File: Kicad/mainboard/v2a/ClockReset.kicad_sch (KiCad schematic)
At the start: 23 parts, among them J9 Conn_01x03_Pin, SW1 RESET Switch, U2 74HC14, U3 74HC590, U4 74HC4040, U5 SST39SF, U6 74HC574, Y1 12 Mhz

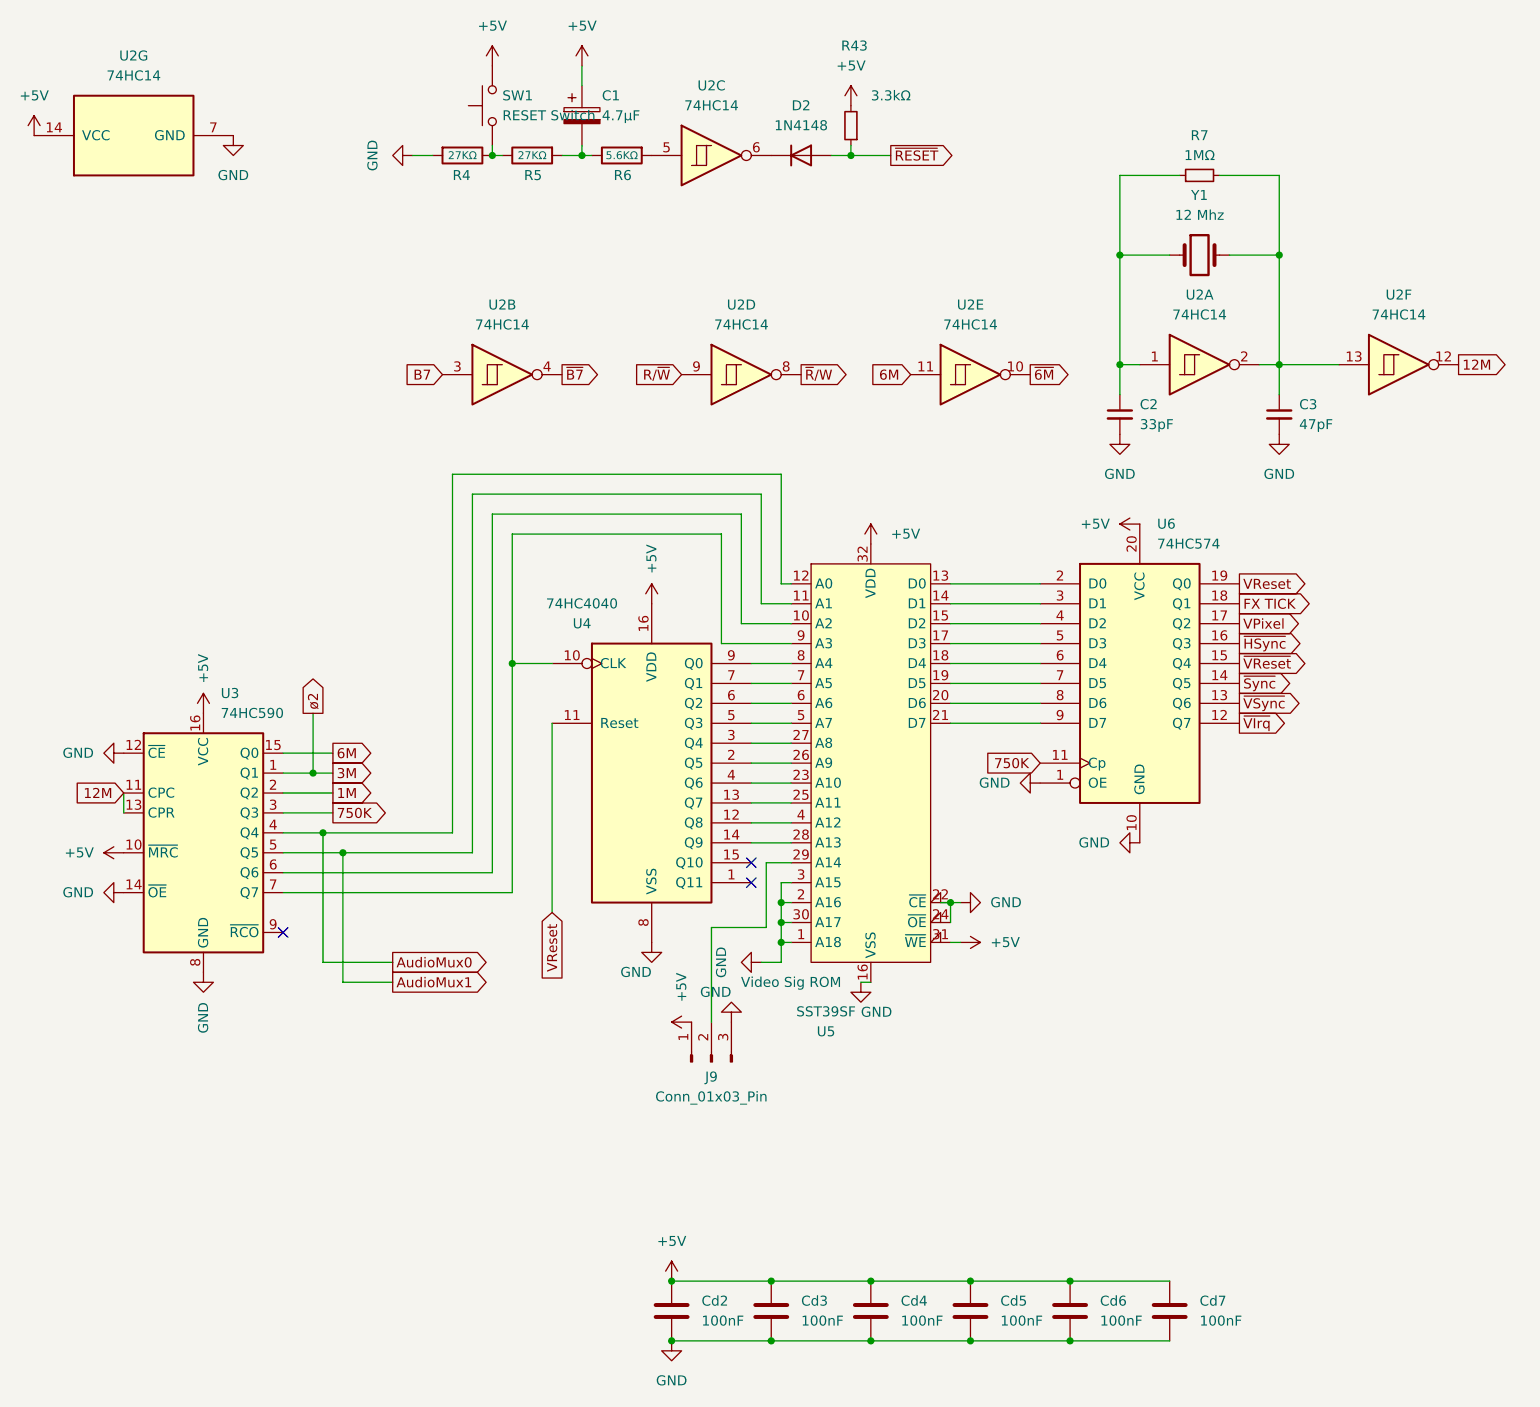
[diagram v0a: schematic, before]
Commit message: Updated pcb files and python scripts
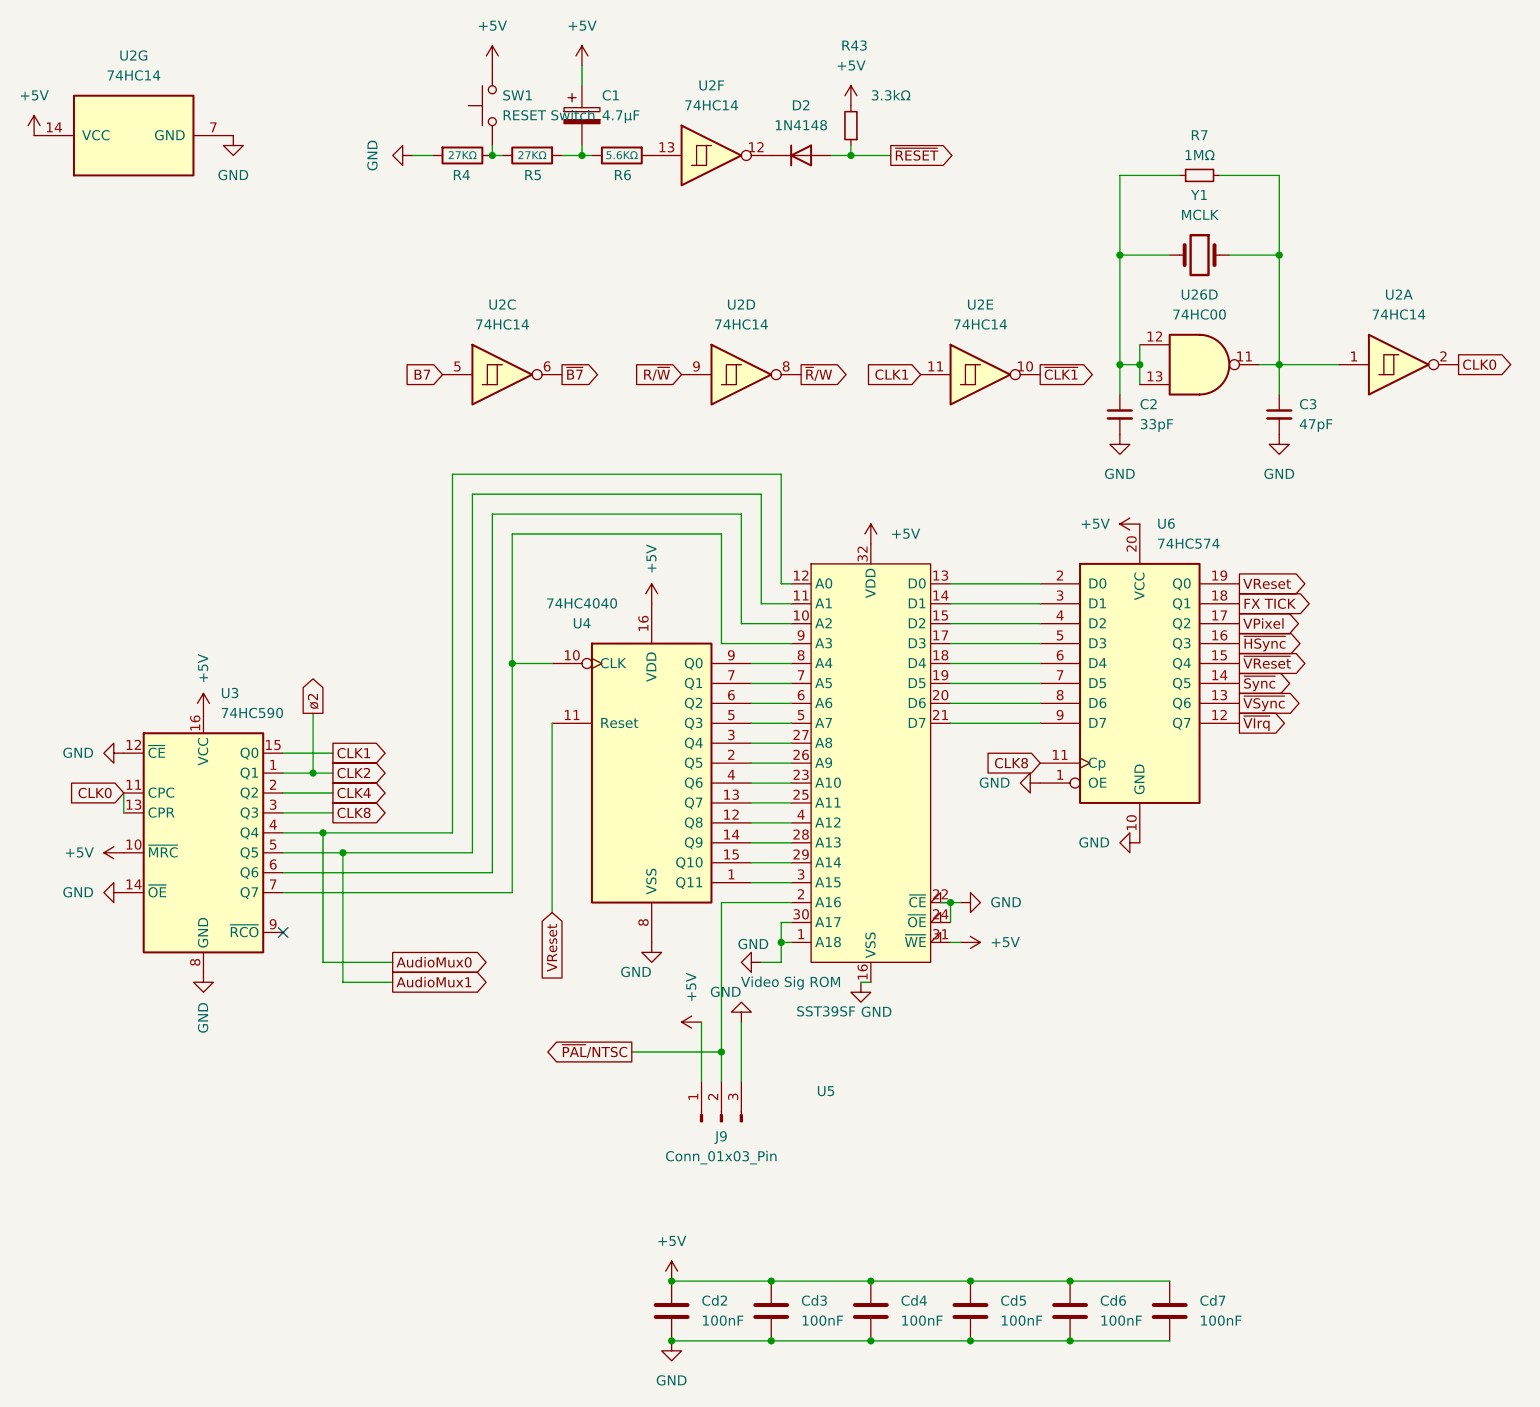
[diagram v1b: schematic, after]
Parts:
- removed unit 2 of U2
- added U26: 74HC00, Smal:DIP-14_W7.62mm_Socket_LongPads_TWEAK, symbol 74xx:74HC00
- U2: footprint PCM_Package_DIP_AKL:DIP-14_W7.62mm_Socket_LongPads -> Smal:DIP-14_W7.62mm_Socket_LongPads_TWEAK
- U3, U4: footprint PCM_Package_DIP_AKL:DIP-16_W7.62mm_Socket_LongPads -> Smal:DIP-16_W7.62mm_Socket_LongPads_TWEAK
- U5: footprint PCM_Package_LCC_AKL:PLCC-32_THT-Socket -> Smal:PLCC-32_THT-Socket_TWEAK
- U6: footprint PCM_Package_DIP_AKL:DIP-20_W7.62mm_Socket_LongPads -> Smal:DIP-20_W7.62mm_Socket_LongPads_TWEAK
- Y1: value 12 Mhz -> MCLK
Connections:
- net B7: now also U2.5
- net GND: no longer U5.2 (A16), U5.3 (A15)
- net ~{B7}: now also U2.6
- net at R6.2: now also U2.13; no longer U2.5
- net at D2.1 (K): now also U2.12; no longer U2.6
- net at U5.29 (A14): now also U4.15 (Q10); no longer J9.2 (Pin_2)
- net at U4.1 (Q11): now also U5.3 (A15)
- net at C2.1, R7.1: now also Y1.2, U26.12, U26.13; no longer U2.1, Y1.1
- net 12M renamed CLK0
- net CLK0: now also U2.2; no longer U2.12
- net 1M renamed CLK4
- net 3M renamed CLK2
- net 6M renamed CLK1
- net 750K renamed CLK8
- net ~{6M} renamed ~{CLK1}
- new net: C3.1, R7.2, U2.1, U26.11, Y1.1
- new net ~{PAL}/NTSC: J9.2 (Pin_2), U5.2 (A16)
- no-connect marks 3 -> 1
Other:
- moved on the sheet: J9, U2A, U2C, U2E, U2F
